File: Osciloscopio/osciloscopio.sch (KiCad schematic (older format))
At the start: 37 parts, among them P1 BNC, Q1 BC557, Q2 BC557, Q3 BC557, Q4 BC557, SW1 SW_PUSH, U4 TL082, U5 CD4066

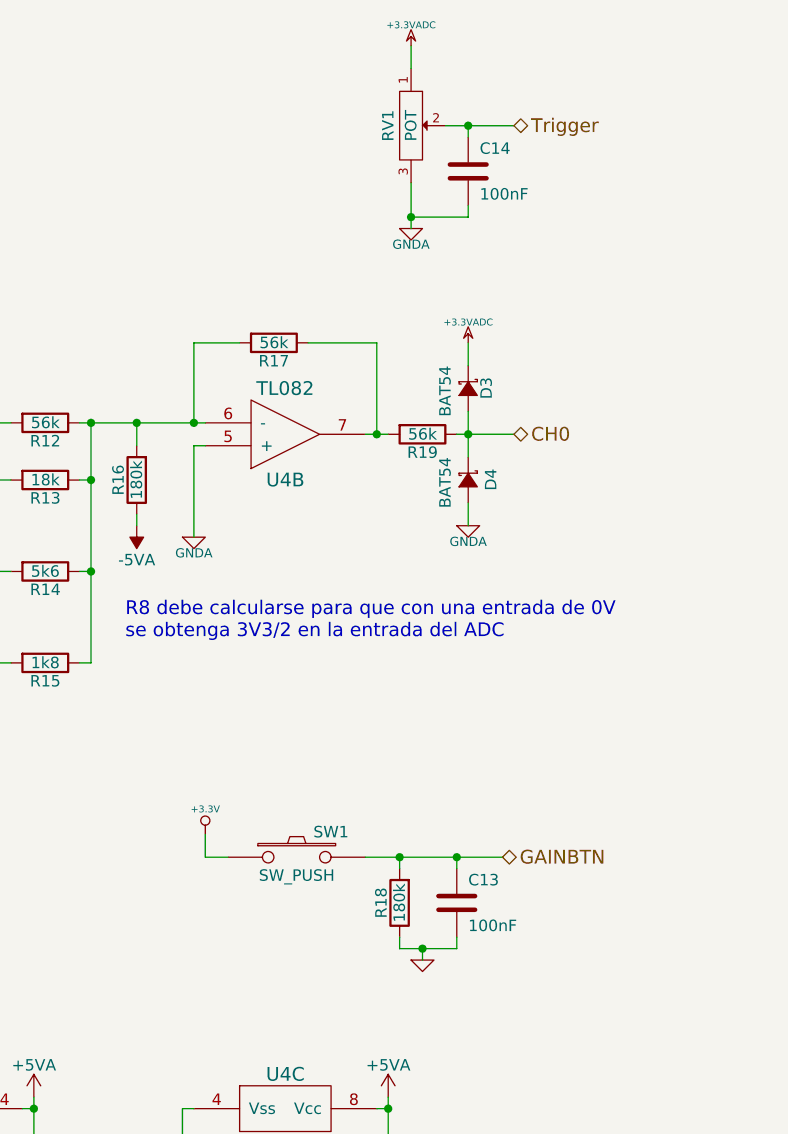
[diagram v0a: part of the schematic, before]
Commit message: Se definen los footprints y numeros de parte de todos los componentes Se elimina el Boton de Gain dado que un solo boton es insuficiente para controlar el osciloscopio y no se disponen de señales digitales suficientes para controlar varios botones. Se decide por ende colocar el display cerca de los botones de la EDU-CIAA de modo que se pueda colocar en el display la función de los botones.
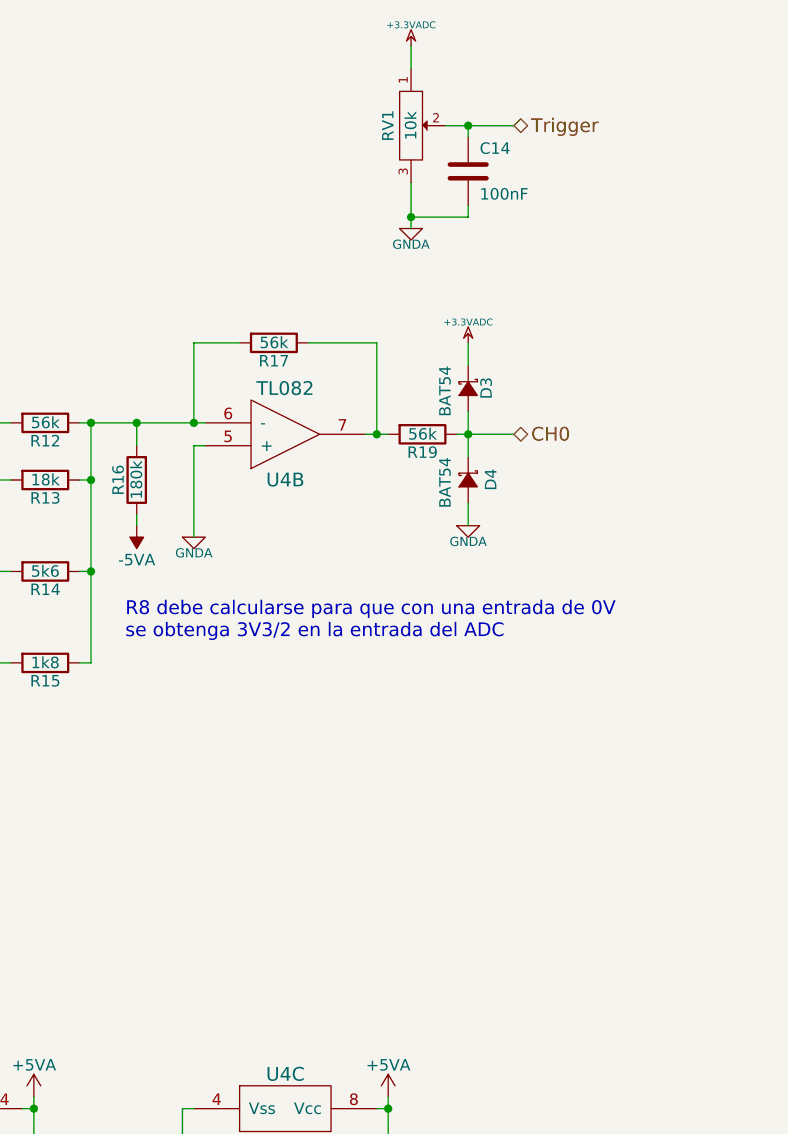
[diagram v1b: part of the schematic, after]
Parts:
- removed C13: 100nF, symbol C
- removed R18: 180k, symbol R
- removed SW1: SW_PUSH, symbol SW_PUSH
- C10, C11, C12, C14: footprint (none) -> Capacitors_SMD:C_0805_HandSoldering; Digikey# (none) -> 1276-6468-1-ND; Manf (none) -> Samsung Electro-Mechanics America, Inc.; Manf# (none) -> CL21B104KBFNNNG
- D1, D2, D3, D4: footprint (none) -> TO_SOT_Packages_SMD:SOT-323; Digikey# (none) -> 568-11592-1-ND; Manf (none) -> NXP Semiconductors; Manf# (none) -> BAT54W,135
- P1: footprint (none) -> Sockets_BNC:BNC_Socket_TYCO-AMP_LargePads; Digikey# (none) -> A32244-ND; Manf (none) -> TE Connectivity AMP Connectors; Manf# (none) -> 5227161-1
- Q1, Q2, Q3, Q4: footprint (none) -> TO_SOT_Packages_THT:TO-92_Inline_Wide; Digikey# (none) -> BC557BTACT-ND; Manf (none) -> Fairchild Semiconductor; Manf# (none) -> BC557BTA
- R1: footprint (none) -> Resistors_SMD:R_0805_HandSoldering; Digikey# (none) -> RMCF0805JG10K0CT-ND; Manf (none) -> Stackpole Electronics Inc.; Manf# (none) -> RMCF0805JG10K0
- R10, R11, R8, R9: footprint (none) -> Resistors_SMD:R_0805_HandSoldering; Digikey# (none) -> RMCF0805JT47K0CT-ND; Manf (none) -> Stackpole Electronics Inc.; Manf# (none) -> RMCF0805JT47K0
- R12, R17, R19: footprint (none) -> Resistors_SMD:R_0805_HandSoldering; Digikey# (none) -> RMCF0805JT56K0CT-ND; Manf (none) -> Stackpole Electronics Inc.; Manf# (none) -> RMCF0805JT56K0
- R13: footprint (none) -> Resistors_SMD:R_0805_HandSoldering; Digikey# (none) -> RMCF0805JT18K0CT-ND; Manf (none) -> Stackpole Electronics Inc.; Manf# (none) -> RMCF0805JT18K0
- R14: footprint (none) -> Resistors_SMD:R_0805_HandSoldering; Digikey# (none) -> RMCF0805JT5K60CT-ND; Manf (none) -> Stackpole Electronics Inc.; Manf# (none) -> RMCF0805JT5K60
- R15: footprint (none) -> Resistors_SMD:R_0805_HandSoldering; Digikey# (none) -> RMCF0805JT1K80CT-ND; Manf (none) -> Stackpole Electronics Inc.; Manf# (none) -> RMCF0805JT1K80
- R16: footprint (none) -> Resistors_SMD:R_0805_HandSoldering; Digikey# (none) -> RMCF0805JT180KTR-ND; Manf (none) -> Stackpole Electronics Inc.; Manf# (none) -> RMCF0805JT180K
- R2, R3, R4, R5, R7: footprint (none) -> Resistors_SMD:R_0805_HandSoldering; Digikey# (none) -> RMCF0805JT100KCT-ND; Manf (none) -> Stackpole Electronics Inc.; Manf# (none) -> RMCF0805JT100K
- R6: footprint (none) -> Resistors_SMD:R_0805_HandSoldering; Digikey# (none) -> RMCF0805JT910KCT-ND; Manf (none) -> Stackpole Electronics Inc.; Manf# (none) -> RMCF0805JT910K
- RV1: value POT -> 10k; footprint (none) -> Potentiometers:Potentiometer_Alps-RK16-single; Manf (none) -> ALPS; Manf# (none) -> RK1631110TBK; Mouser# (none) -> 688-RK1631110TBK
- U4: footprint (none) -> Housings_DIP:DIP-8_W7.62mm_LongPads
- U5: footprint (none) -> Housings_DIP:DIP-14_W7.62mm_LongPads

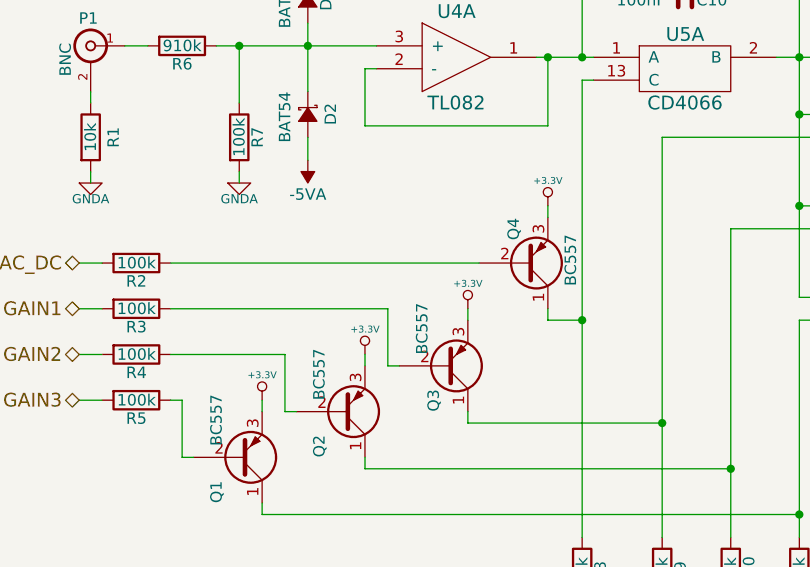
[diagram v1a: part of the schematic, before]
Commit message: Se realiza el Placement de los componentes y un prerouteo para mostrar que el placement elegido permite un adecuado routeo del mismo.
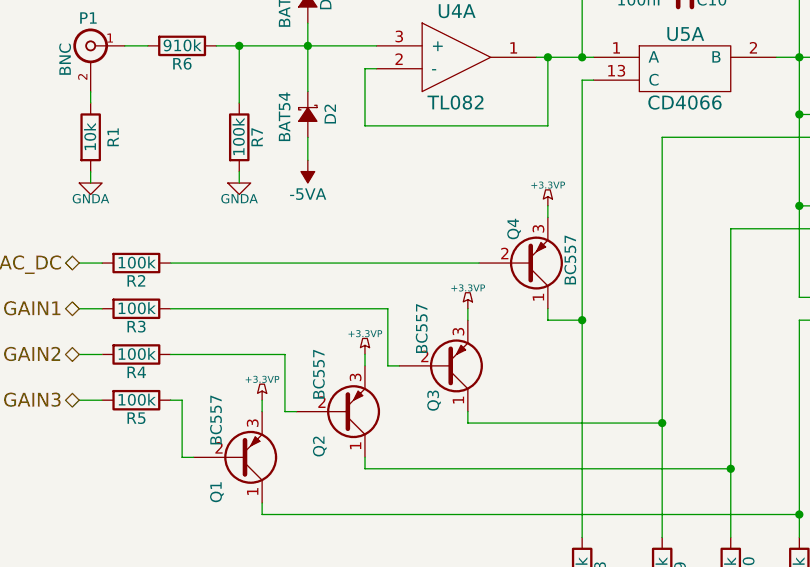
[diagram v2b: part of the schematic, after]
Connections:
- net +3.3V renamed +3.3VP
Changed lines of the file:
@@
-$EndComp
-$Comp
-L +3.3V #PWR016
-U 1 1 57834308
-P 4050 3550
-F 0 "#PWR016" H 4050 3510 30  0001 C CNN
-F 1 "+3.3V" H 4050 3660 30  0000 C CNN
-F 2 "" H 4050 3550 60  0000 C CNN
-F 3 "" H 4050 3550 60  0000 C CNN
-	1    4050 3550
-	1    0    0    -1
 $EndComp
 $Comp
@@
 $EndComp
 $Comp
-L +3.3V #PWR017
-U 1 1 57834364
-P 3600 3750
-F 0 "#PWR017" H 3600 3710 30  0001 C CNN
-F 1 "+3.3V" H 3600 3860 30  0000 C CNN
-F 2 "" H 3600 3750 60  0000 C CNN
-F 3 "" H 3600 3750 60  0000 C CNN
-	1    3600 3750
-	1    0    0    -1
-$EndComp
-$Comp
 L Q_PNP_CBE Q4
 U 1 1 5783436A
@@
 $EndComp
 $Comp
-L +3.3V #PWR018
-U 1 1 57834371
-P 4400 3100
-F 0 "#PWR018" H 4400 3060 30  0001 C CNN
-F 1 "+3.3V" H 4400 3210 30  0000 C CNN
-F 2 "" H 4400 3100 60  0000 C CNN
-F 3 "" H 4400 3100 60  0000 C CNN
-	1    4400 3100
-	1    0    0    -1
-$EndComp
-$Comp
 L Q_PNP_CBE Q1
 U 1 1 57834377
@@
 $EndComp
 $Comp
-L +3.3V #PWR019
-U 1 1 5783437E
-P 3150 3950
-F 0 "#PWR019" H 3150 3910 30  0001 C CNN
-F 1 "+3.3V" H 3150 4060 30  0000 C CNN
-F 2 "" H 3150 3950 60  0000 C CNN
-F 3 "" H 3150 3950 60  0000 C CNN
-	1    3150 3950
-	1    0    0    -1
-$EndComp
-$Comp
 L R R4
 U 1 1 57834384
@@
 	0    1    1    0
 $EndComp
+$Comp
+L +3.3VP #PWR?
+U 1 1 578EE56D
+P 4400 3100
+F 0 "#PWR?" H 4450 3130 20  0001 C CNN
+F 1 "+3.3VP" H 4400 3190 30  0000 C CNN
+F 2 "" H 4400 3100 60  0000 C CNN
+F 3 "" H 4400 3100 60  0000 C CNN
+	1    4400 3100
+	1    0    0    -1
+$EndComp
+$Comp
+L +3.3VP #PWR?
+U 1 1 578EE8DA
+P 4050 3550
+F 0 "#PWR?" H 4100 3580 20  0001 C CNN
+F 1 "+3.3VP" H 4050 3640 30  0000 C CNN
+F 2 "" H 4050 3550 60  0000 C CNN
+F 3 "" H 4050 3550 60  0000 C CNN
+	1    4050 3550
+	1    0    0    -1
+$EndComp
+$Comp
+L +3.3VP #PWR?
+U 1 1 578EE9A6
+P 3600 3750
+F 0 "#PWR?" H 3650 3780 20  0001 C CNN
+F 1 "+3.3VP" H 3600 3840 30  0000 C CNN
+F 2 "" H 3600 3750 60  0000 C CNN
+F 3 "" H 3600 3750 60  0000 C CNN
+	1    3600 3750
+	1    0    0    -1
+$EndComp
+$Comp
+L +3.3VP #PWR?
+U 1 1 578EE9D4
+P 3150 3950
+F 0 "#PWR?" H 3200 3980 20  0001 C CNN
+F 1 "+3.3VP" H 3150 4040 30  0000 C CNN
+F 2 "" H 3150 3950 60  0000 C CNN
+F 3 "" H 3150 3950 60  0000 C CNN
+	1    3150 3950
+	1    0    0    -1
+$EndComp
 $EndSCHEMATC

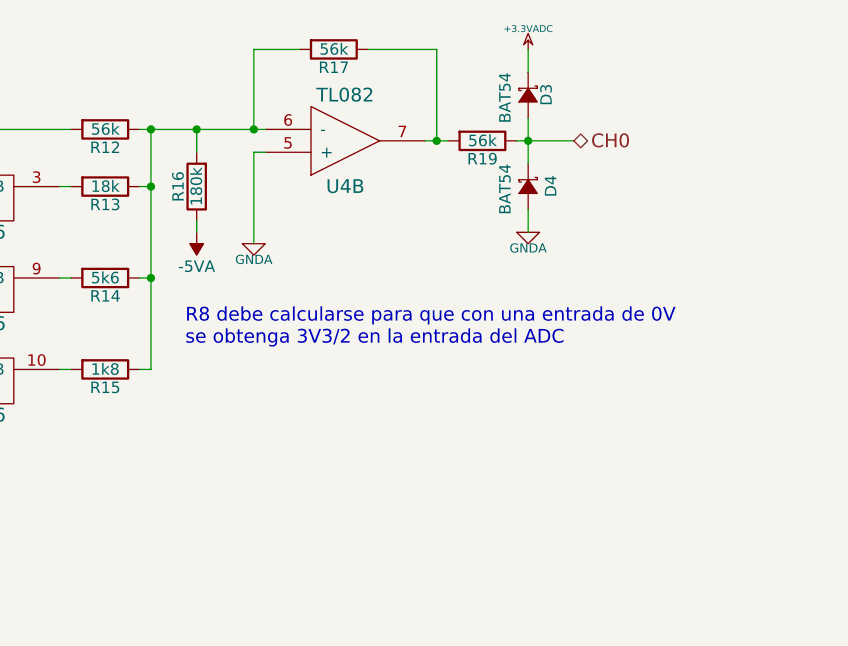
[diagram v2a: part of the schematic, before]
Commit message: Se finaliza el prerouteo y se realizan las primeras correcciones de la revision
Este routeo cumple chequeo de DRC pero no es definitivo, le faltan planos y detalles finos.

Se realiza este commit antes de continuar con los demas cambios sugeridos por la revisión que son más peligrosos, como quitar una hoja del esquematico y quitar todos aquellos pines del AX1 que no se están utilizando
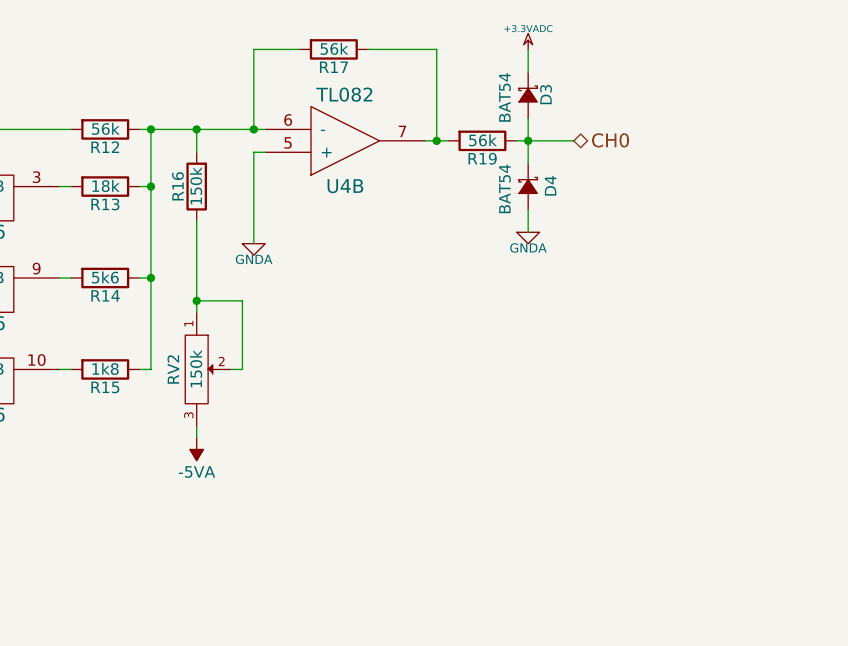
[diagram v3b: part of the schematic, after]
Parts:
- added RV2: 150k, Potentiometers:Potentiometer_Bourns_3296W_3-8Zoll_Inline_ScrewUp, symbol POT
- R16: value 180k -> 150k; Digikey# RMCF0805JT180KTR-ND -> RMCF0805JT150KCT-ND; Manf# RMCF0805JT180K -> RMCF0805JT150K
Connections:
- net -5VA: now also RV2.3; no longer R16.1
- new net: R16.1, RV2.1, RV2.2
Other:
- note removed: "R8 debe calcularse para que con una entrada de 0V\nse obtenga 3V3/2 en la entrada del ADC"

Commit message: Routeo Definitivo
Queda pendiente volver locales los footprints y reparar el 3D de la placa
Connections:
- net OscGND: now reaches P1.2 (Ext), R1.1
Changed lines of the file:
@@
 $Descr A4 11693 8268
 encoding utf-8
-Sheet 4 5
+Sheet 3 5
 Title "Poncho Osciloscopio"
 Date ""
@@
 AR Path="/560A0C1A/57832D16/578342B4" Ref="R6"  Part="1"
 AR Path="/579AD191/578342B4" Ref="R6"  Part="1"
-F 0 "R6" V 2880 2400 50  0000 C CNN
+F 0 "R6" V 2700 2400 50  0000 C CNN
 F 1 "910k" V 2800 2400 50  0000 C CNN
 F 2 "Resistors_SMD:R_0805_HandSoldering" V 2730 2400 50  0001 C CNN
@@
 Wire Wire Line
 	6950 3800 6950 3750
+Wire Wire Line
+	2400 2600 2800 2600
+Text Label 2450 2600 0    60   ~ 0
+OscGND
 $EndSCHEMATC

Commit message: Ultimas correciones de la revisión
_ Se copian localmente footprints y se los linkead
_ Se copian localmente los modelos 3D y se los linkea
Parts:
- C10, C11, C12, C14: footprint Capacitors_SMD:C_0805_HandSoldering -> osc:C_0805_HandSoldering
- D1, D2, D3, D4: footprint TO_SOT_Packages_SMD:SOT-323 -> osc:SOT-323
- P1: footprint Sockets_BNC:BNC_Socket_TYCO-AMP_LargePads -> osc:BNC_Socket_TYCO-AMP_LargePads
- Q1, Q2, Q3, Q4: footprint TO_SOT_Packages_THT:TO-92_Inline_Wide -> osc:TO-92_Inline_Wide
- R1, R10, R11, R12, R13, R14, R15, R16, R17, R19, R2, R3, R4, R5, R6, R7, R8, R9: footprint Resistors_SMD:R_0805_HandSoldering -> osc:R_0805_HandSoldering
- RV1: footprint Potentiometers:Potentiometer_Alps-RK16-single -> osc:Potentiometer_Alps-RK16-single
- RV2: footprint Potentiometers:Potentiometer_Bourns_3296W_3-8Zoll_Inline_ScrewUp -> osc:Potentiometer_Bourns_3296W_3-8Zoll_Inline_ScrewUp
- U4: footprint Housings_DIP:DIP-8_W7.62mm_LongPads -> osc:DIP-8_W7.62mm_LongPads
- U5: footprint Housings_DIP:DIP-14_W7.62mm_LongPads -> osc:DIP-14_W7.62mm_LongPads
